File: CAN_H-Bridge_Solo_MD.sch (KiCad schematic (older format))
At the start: 45 parts, among them IC1 SI8650AB-B-IS1, IC2 A3921KLPTR-T, J2 Conn_01x03, J3 Conn_01x05, J4 Bus_mechaken_PCIexpress_x16_1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, M1 Motor_DC, Q1 IRLB3813PBF, Q2 IRLB3813PBF, Q3 IRLB3813PBF, Q4 IRLB3813PBF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

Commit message: change
FETのドレイン端子を移動
パッドを手はんだ用に変更
PCIeコネクタを変更
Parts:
- C1, C10, C11, C12, C13, C2, C3, C4, C5, C6, C7, C8, C9: footprint Capacitor_SMD:C_0805_2012Metric -> Capacitor_SMD:C_0805_2012Metric_Pad1.15x1.40mm_HandSolder
- D1, D2, D3, D4: footprint LED_SMD:LED_0603_1608Metric -> LED_SMD:LED_0603_1608Metric_Castellated
- D5: footprint Diode_SMD:D_0603_1608Metric -> LED_SMD:LED_0603_1608Metric_Castellated
- J4: footprint PCIe:BUS_mechaken_PCIexpress_x16_164_Position -> PCIe:BUS_mechaken_PCIexpress_x16
- R1, R10, R11, R12, R2, R3, R4, R5, R6, R7, R8, R9: footprint Resistor_SMD:R_0603_1608Metric -> Resistor_SMD:R_0603_1608Metric_Pad1.05x0.95mm_HandSolder
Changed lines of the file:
@@
 F 0 "R10" H 10470 4946 50  0000 L CNN
 F 1 "3K" H 10470 4855 50  0000 L CNN
-F 2 "Resistor_SMD:R_0603_1608Metric" V 10330 4900 50  0001 C CNN
+F 2 "Resistor_SMD:R_0603_1608Metric_Pad1.05x0.95mm_HandSolder" V 10330 4900 50  0001 C CNN
 F 3 "~" H 10400 4900 50  0001 C CNN
 	1    10400 4900
@@
 F 0 "R12" H 10930 4854 50  0000 R CNN
 F 1 "2.2k" H 10930 4945 50  0000 R CNN
-F 2 "Resistor_SMD:R_0603_1608Metric" V 10930 4900 50  0001 C CNN
+F 2 "Resistor_SMD:R_0603_1608Metric_Pad1.05x0.95mm_HandSolder" V 10930 4900 50  0001 C CNN
 F 3 "~" H 11000 4900 50  0001 C CNN
 	1    11000 4900
@@
 F 0 "R11" H 10770 4946 50  0000 L CNN
 F 1 "10k" H 10770 4855 50  0000 L CNN
-F 2 "Resistor_SMD:R_0603_1608Metric" V 10630 4900 50  0001 C CNN
+F 2 "Resistor_SMD:R_0603_1608Metric_Pad1.05x0.95mm_HandSolder" V 10630 4900 50  0001 C CNN
 F 3 "~" H 10700 4900 50  0001 C CNN
 	1    10700 4900
@@
 F 0 "C12" H 10015 5446 50  0000 L CNN
 F 1 "0.1uF" H 10015 5355 50  0000 L CNN
-F 2 "Capacitor_SMD:C_0805_2012Metric" H 9938 5250 50  0001 C CNN
+F 2 "Capacitor_SMD:C_0805_2012Metric_Pad1.15x1.40mm_HandSolder" H 9938 5250 50  0001 C CNN
 F 3 "~" H 9900 5400 50  0001 C CNN
 	1    9900 5400
@@
 F 0 "C9" H 7565 5846 50  0000 L CNN
 F 1 "0.1uF" H 7565 5755 50  0000 L CNN
-F 2 "Capacitor_SMD:C_0805_2012Metric" H 7488 5650 50  0001 C CNN
+F 2 "Capacitor_SMD:C_0805_2012Metric_Pad1.15x1.40mm_HandSolder" H 7488 5650 50  0001 C CNN
 F 3 "~" H 7450 5800 50  0001 C CNN
 	1    7450 5800
@@
 F 0 "D5" H 7300 5866 50  0000 C CNN
 F 1 "D" H 7300 5775 50  0000 C CNN
-F 2 "Diode_SMD:D_0603_1608Metric" H 7300 5650 50  0001 C CNN
+F 2 "LED_SMD:LED_0603_1608Metric_Castellated" H 7300 5650 50  0001 C CNN
 F 3 "~" H 7300 5650 50  0001 C CNN
 	1    7300 5650
@@
 F 0 "C5" V 5648 3950 50  0000 C CNN
 F 1 "0.1uF" V 5739 3950 50  0000 C CNN
-F 2 "Capacitor_SMD:C_0805_2012Metric" H 5938 3800 50  0001 C CNN
+F 2 "Capacitor_SMD:C_0805_2012Metric_Pad1.15x1.40mm_HandSolder" H 5938 3800 50  0001 C CNN
 F 3 "~" H 5900 3950 50  0001 C CNN
 	1    5900 3950
@@
 F 0 "C4" V 4248 4600 50  0000 C CNN
 F 1 "0.1uF" V 4339 4600 50  0000 C CNN
-F 2 "Capacitor_SMD:C_0805_2012Metric" H 4538 4450 50  0001 C CNN
+F 2 "Capacitor_SMD:C_0805_2012Metric_Pad1.15x1.40mm_HandSolder" H 4538 4450 50  0001 C CNN
 F 3 "~" H 4500 4600 50  0001 C CNN
 	1    4500 4600
@@
 F 0 "C1" V 748 1800 50  0000 C CNN
 F 1 "1uF" V 839 1800 50  0000 C CNN
-F 2 "Capacitor_SMD:C_0805_2012Metric" H 1038 1650 50  0001 C CNN
+F 2 "Capacitor_SMD:C_0805_2012Metric_Pad1.15x1.40mm_HandSolder" H 1038 1650 50  0001 C CNN
 F 3 "~" H 1000 1800 50  0001 C CNN
 	1    1000 1800
@@
 F 0 "C2" V 1448 1800 50  0000 C CNN
 F 1 "4.7uF" V 1539 1800 50  0000 C CNN
-F 2 "Capacitor_SMD:C_0805_2012Metric" H 1738 1650 50  0001 C CNN
+F 2 "Capacitor_SMD:C_0805_2012Metric_Pad1.15x1.40mm_HandSolder" H 1738 1650 50  0001 C CNN
 F 3 "~" H 1700 1800 50  0001 C CNN
 	1    1700 1800
@@
 F 0 "D1" V 1039 3450 50  0000 C CNN
 F 1 "LED" V 948 3450 50  0000 C CNN
-F 2 "LED_SMD:LED_0603_1608Metric" H 1000 3300 50  0001 C CNN
+F 2 "LED_SMD:LED_0603_1608Metric_Castellated" H 1000 3300 50  0001 C CNN
 F 3 "~" H 1000 3300 50  0001 C CNN
 	1    1000 3300
@@
 F 0 "C3" V 3848 1150 50  0000 C CNN
 F 1 "0.1uF" V 3939 1150 50  0000 C CNN
-F 2 "Capacitor_SMD:C_0805_2012Metric" H 4138 1000 50  0001 C CNN
+F 2 "Capacitor_SMD:C_0805_2012Metric_Pad1.15x1.40mm_HandSolder" H 4138 1000 50  0001 C CNN
 F 3 "~" H 4100 1150 50  0001 C CNN
 	1    4100 1150
@@
 F 0 "R5" V 2443 3100 50  0000 C CNN
 F 1 "10K" V 2534 3100 50  0000 C CNN
-F 2 "Resistor_SMD:R_0603_1608Metric" V 2580 3100 50  0001 C CNN
+F 2 "Resistor_SMD:R_0603_1608Metric_Pad1.05x0.95mm_HandSolder" V 2580 3100 50  0001 C CNN
 F 3 "~" H 2650 3100 50  0001 C CNN
 	1    2650 3100
@@
 F 0 "C7" H 7264 4854 50  0000 L CNN
 F 1 "4.7uF" H 7264 4945 50  0000 L CNN
-F 2 "Capacitor_SMD:C_0805_2012Metric" H 7188 4750 50  0001 C CNN
+F 2 "Capacitor_SMD:C_0805_2012Metric_Pad1.15x1.40mm_HandSolder" H 7188 4750 50  0001 C CNN
 F 3 "~" H 7150 4900 50  0001 C CNN
 	1    7150 4900
@@
 F 0 "C8" H 6823 5446 50  0000 L CNN
 F 1 "4.7uF" H 6823 5355 50  0000 L CNN
-F 2 "Capacitor_SMD:C_0805_2012Metric" H 7188 5250 50  0001 C CNN
+F 2 "Capacitor_SMD:C_0805_2012Metric_Pad1.15x1.40mm_HandSolder" H 7188 5250 50  0001 C CNN
 F 3 "~" H 7150 5400 50  0001 C CNN
 	1    7150 5400
@@
 F 0 "C10" H 9074 5754 50  0000 L CNN
 F 1 "0.47uF" H 9074 5845 50  0000 L CNN
-F 2 "Capacitor_SMD:C_0805_2012Metric" H 9488 5650 50  0001 C CNN
+F 2 "Capacitor_SMD:C_0805_2012Metric_Pad1.15x1.40mm_HandSolder" H 9488 5650 50  0001 C CNN
 F 3 "~" H 9450 5800 50  0001 C CNN
 	1    9450 5800
@@
 F 0 "R4" V 2550 6974 50  0000 L CNN
 F 1 "21" V 2450 6974 50  0000 L CNN
-F 2 "Resistor_SMD:R_0603_1608Metric" V 2280 7050 50  0001 C CNN
+F 2 "Resistor_SMD:R_0603_1608Metric_Pad1.05x0.95mm_HandSolder" V 2280 7050 50  0001 C CNN
 F 3 "~" H 2350 7050 50  0001 C CNN
 	1    2350 7050
@@
 F 0 "C6" H 6415 5046 50  0000 L CNN
 F 1 "4.7uF" H 6415 4955 50  0000 L CNN
-F 2 "Capacitor_SMD:C_0805_2012Metric" H 6338 4850 50  0001 C CNN
+F 2 "Capacitor_SMD:C_0805_2012Metric_Pad1.15x1.40mm_HandSolder" H 6338 4850 50  0001 C CNN
 F 3 "~" H 6300 5000 50  0001 C CNN
 	1    6300 5000
@@
 F 0 "D4" V 3939 5133 50  0000 R CNN
 F 1 "LED" V 3848 5133 50  0000 R CNN
-F 2 "LED_SMD:LED_0603_1608Metric" H 3900 5250 50  0001 C CNN
+F 2 "LED_SMD:LED_0603_1608Metric_Castellated" H 3900 5250 50  0001 C CNN
 F 3 "~" H 3900 5250 50  0001 C CNN
 	1    3900 5250
@@
 F 0 "D3" V 3589 5133 50  0000 R CNN
 F 1 "LED" V 3498 5133 50  0000 R CNN
-F 2 "LED_SMD:LED_0603_1608Metric" H 3550 5250 50  0001 C CNN
+F 2 "LED_SMD:LED_0603_1608Metric_Castellated" H 3550 5250 50  0001 C CNN
 F 3 "~" H 3550 5250 50  0001 C CNN
 	1    3550 5250
@@
 F 0 "J4" H 7600 6800 50  0000 C CNN
 F 1 "Bus_mechaken_PCIexpress_x16_164_Position" H 7550 5400 50  0000 C CNN
-F 2 "PCIe:BUS_mechaken_PCIexpress_x16_164_Position" H 7250 3600 50  0001 C CNN
+F 2 "PCIe:BUS_mechaken_PCIexpress_x16" H 7250 3600 50  0001 C CNN
 F 3 "http://pinouts.ru/Slots/PCI_pinout.shtml" H 7250 3600 50  0001 C CNN
 	1    7600 3700
@@
 F 0 "C11" V 9648 3150 50  0000 C CNN
 F 1 "1uF" V 9739 3150 50  0000 C CNN
-F 2 "Capacitor_SMD:C_0805_2012Metric" H 9938 3000 50  0001 C CNN
+F 2 "Capacitor_SMD:C_0805_2012Metric_Pad1.15x1.40mm_HandSolder" H 9938 3000 50  0001 C CNN
 F 3 "~" H 9900 3150 50  0001 C CNN
 	1    9900 3150
@@
 F 0 "C13" V 10348 3150 50  0000 C CNN
 F 1 "4.7uF" V 10439 3150 50  0000 C CNN
-F 2 "Capacitor_SMD:C_0805_2012Metric" H 10638 3000 50  0001 C CNN
+F 2 "Capacitor_SMD:C_0805_2012Metric_Pad1.15x1.40mm_HandSolder" H 10638 3000 50  0001 C CNN
 F 3 "~" H 10600 3150 50  0001 C CNN
 	1    10600 3150
@@
 F 0 "R2" H 1370 2896 50  0000 L CNN
 F 1 "2.2K" H 1370 2805 50  0000 L CNN
-F 2 "Resistor_SMD:R_0603_1608Metric" V 1230 2850 50  0001 C CNN
+F 2 "Resistor_SMD:R_0603_1608Metric_Pad1.05x0.95mm_HandSolder" V 1230 2850 50  0001 C CNN
 F 3 "~" H 1300 2850 50  0001 C CNN
 	1    1300 2850
@@
 F 0 "R1" H 1070 2896 50  0000 L CNN
 F 1 "2.2K" H 1070 2805 50  0000 L CNN
-F 2 "Resistor_SMD:R_0603_1608Metric" V 930 2850 50  0001 C CNN
+F 2 "Resistor_SMD:R_0603_1608Metric_Pad1.05x0.95mm_HandSolder" V 930 2850 50  0001 C CNN
 F 3 "~" H 1000 2850 50  0001 C CNN
 	1    1000 2850
@@
 F 0 "D2" V 1339 3112 50  0000 C CNN
 F 1 "LED" V 1248 3112 50  0000 C CNN
-F 2 "LED_SMD:LED_0603_1608Metric" H 1300 3300 50  0001 C CNN
+F 2 "LED_SMD:LED_0603_1608Metric_Castellated" H 1300 3300 50  0001 C CNN
 F 3 "~" H 1300 3300 50  0001 C CNN
 	1    1300 3300
@@
 F 0 "R9" V 4815 6975 50  0000 L CNN
 F 1 "21" V 4906 6975 50  0000 L CNN
-F 2 "Resistor_SMD:R_0603_1608Metric" V 4630 7050 50  0001 C CNN
+F 2 "Resistor_SMD:R_0603_1608Metric_Pad1.05x0.95mm_HandSolder" V 4630 7050 50  0001 C CNN
 F 3 "~" H 4700 7050 50  0001 C CNN
 	1    4700 7050
@@
 F 0 "R3" V 2550 6275 50  0000 L CNN
 F 1 "21" V 2450 6275 50  0000 L CNN
-F 2 "Resistor_SMD:R_0603_1608Metric" V 2280 6350 50  0001 C CNN
+F 2 "Resistor_SMD:R_0603_1608Metric_Pad1.05x0.95mm_HandSolder" V 2280 6350 50  0001 C CNN
 F 3 "~" H 2350 6350 50  0001 C CNN
 	1    2350 6350
@@
 F 0 "R8" V 4815 6276 50  0000 L CNN
 F 1 "21" V 4906 6276 50  0000 L CNN
-F 2 "Resistor_SMD:R_0603_1608Metric" V 4630 6350 50  0001 C CNN
+F 2 "Resistor_SMD:R_0603_1608Metric_Pad1.05x0.95mm_HandSolder" V 4630 6350 50  0001 C CNN
 F 3 "~" H 4700 6350 50  0001 C CNN
 	1    4700 6350
@@
 F 0 "R6" H 3620 4996 50  0000 L CNN
 F 1 "2.2K" H 3620 4905 50  0000 L CNN
-F 2 "Resistor_SMD:R_0603_1608Metric" V 3480 4950 50  0001 C CNN
+F 2 "Resistor_SMD:R_0603_1608Metric_Pad1.05x0.95mm_HandSolder" V 3480 4950 50  0001 C CNN
 F 3 "~" H 3550 4950 50  0001 C CNN
 	1    3550 4950
@@
 F 0 "R7" H 3970 4996 50  0000 L CNN
 F 1 "2.2K" H 3970 4905 50  0000 L CNN
-F 2 "Resistor_SMD:R_0603_1608Metric" V 3830 4950 50  0001 C CNN
+F 2 "Resistor_SMD:R_0603_1608Metric_Pad1.05x0.95mm_HandSolder" V 3830 4950 50  0001 C CNN
 F 3 "~" H 3900 4950 50  0001 C CNN
 	1    3900 4950

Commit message: change
レギュレータを新規に追加
その他細かな修正
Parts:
- added C14: 2.2u, Capacitor_SMD:C_0805_2012Metric_Pad1.15x1.40mm_HandSolder, symbol Device:C
- added C15: 1u, Capacitor_SMD:C_0805_2012Metric_Pad1.15x1.40mm_HandSolder, symbol Device:C
- added IC3: AP7381-50SA-7, SOT96P240X105-3N, symbol SamacSys_Parts:AP7381-50SA-7
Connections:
- wire segments 101 -> 107
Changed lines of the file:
@@
 	1    0    0    -1
 $EndComp
+$Comp
+L SamacSys_Parts:AP7381-50SA-7 IC3
+U 1 1 5E2DF031
+P 9650 2200
+F 0 "IC3" H 10200 2465 50  0000 C CNN
+F 1 "AP7381-50SA-7" H 10200 2374 50  0000 C CNN
+F 2 "SOT96P240X105-3N" H 10600 2300 50  0001 L CNN
+F 3 "https://componentsearchengine.com/Datasheets/1/AP7381-50SA-7.pdf" H 10600 2200 50  0001 L CNN
+F 4 "LDO Voltage Regulators LDO CMOS LowCurr SOT23 T&R 3K" H 10600 2100 50  0001 L CNN "Description"
+F 5 "1.05" H 10600 2000 50  0001 L CNN "Height"
+F 6 "621-AP7381-50SA-7" H 10600 1900 50  0001 L CNN "Mouser Part Number"
+F 7 "https://www.mouser.com/Search/Refine.aspx?Keyword=621-AP7381-50SA-7" H 10600 1800 50  0001 L CNN "Mouser Price/Stock"
+F 8 "Diodes Inc." H 10600 1700 50  0001 L CNN "Manufacturer_Name"
+F 9 "AP7381-50SA-7" H 10600 1600 50  0001 L CNN "Manufacturer_Part_Number"
+	1    9650 2200
+	1    0    0    -1
+$EndComp
+$Comp
+L power:GNDPWR #PWR0101
+U 1 1 5E2DFCDA
+P 10750 2600
+F 0 "#PWR0101" H 10750 2400 50  0001 C CNN
+F 1 "GNDPWR" H 10754 2446 50  0000 C CNN
+F 2 "" H 10750 2550 50  0001 C CNN
+F 3 "" H 10750 2550 50  0001 C CNN
+	1    10750 2600
+	1    0    0    -1
+$EndComp
+$Comp
+L Device:C C15
+U 1 1 5E2E38F9
+P 9400 2350
+F 0 "C15" H 9285 2304 50  0000 R CNN
+F 1 "1u" H 9285 2395 50  0000 R CNN
+F 2 "Capacitor_SMD:C_0805_2012Metric_Pad1.15x1.40mm_HandSolder" H 9438 2200 50  0001 C CNN
+F 3 "~" H 9400 2350 50  0001 C CNN
+	1    9400 2350
+	-1   0    0    1
+$EndComp
+$Comp
+L Device:C C14
+U 1 1 5E2E6C2C
+P 9200 2450
+F 0 "C14" H 9315 2404 50  0000 L CNN
+F 1 "2.2u" H 9315 2495 50  0000 L CNN
+F 2 "Capacitor_SMD:C_0805_2012Metric_Pad1.15x1.40mm_HandSolder" H 9238 2300 50  0001 C CNN
+F 3 "~" H 9200 2450 50  0001 C CNN
+	1    9200 2450
+	-1   0    0    1
+$EndComp
+Wire Wire Line
+	9650 2200 9400 2200
+Wire Wire Line
+	9200 2600 9400 2600
+Wire Wire Line
+	10750 2600 10750 2200
+Connection ~ 10750 2600
+Wire Wire Line
+	9200 2300 9650 2300
+Wire Wire Line
+	9400 2500 9400 2600
+Connection ~ 9400 2600
+Wire Wire Line
+	9400 2600 10750 2600
+$Comp
+L power:VCC #PWR011
+U 1 1 5E308F85
+P 9400 2200
+F 0 "#PWR011" H 9400 2050 50  0001 C CNN
+F 1 "VCC" H 9417 2373 50  0000 C CNN
+F 2 "" H 9400 2200 50  0001 C CNN
+F 3 "" H 9400 2200 50  0001 C CNN
+	1    9400 2200
+	0    -1   -1   0
+$EndComp
+Text GLabel 9200 2300 0    50   Output ~ 0
+MD_3V3
 $EndSCHEMATC

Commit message: clean
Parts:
- IC3: symbol SamacSys_Parts:AP7381-50SA-7 -> CAN_H-Bridge_Solo_MD-rescue:AP7381-50SA-7-SamacSys_Parts
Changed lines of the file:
@@
 $EndComp
 $Comp
-L SamacSys_Parts:AP7381-50SA-7 IC3
+L CAN_H-Bridge_Solo_MD-rescue:AP7381-50SA-7-SamacSys_Parts IC3
 U 1 1 5E2DF031
 P 9650 2200

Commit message: release
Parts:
- Q1, Q2, Q3, Q4: value IRLB3813PBF -> IRFB3806PBF
- R1, R2, R6, R7: value 2.2K -> 2.2k
- R10: value 3K -> 3k
- R5: value 10K -> 10k
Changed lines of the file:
@@
 P 10400 4900
 F 0 "R10" H 10470 4946 50  0000 L CNN
-F 1 "3K" H 10470 4855 50  0000 L CNN
+F 1 "3k" H 10470 4855 50  0000 L CNN
 F 2 "Resistor_SMD:R_0603_1608Metric_Pad1.05x0.95mm_HandSolder" V 10330 4900 50  0001 C CNN
 F 3 "~" H 10400 4900 50  0001 C CNN
@@
 P 2650 3100
 F 0 "R5" V 2443 3100 50  0000 C CNN
-F 1 "10K" V 2534 3100 50  0000 C CNN
+F 1 "10k" V 2534 3100 50  0000 C CNN
 F 2 "Resistor_SMD:R_0603_1608Metric_Pad1.05x0.95mm_HandSolder" V 2580 3100 50  0001 C CNN
 F 3 "~" H 2650 3100 50  0001 C CNN
@@
 P 1300 2850
 F 0 "R2" H 1370 2896 50  0000 L CNN
-F 1 "2.2K" H 1370 2805 50  0000 L CNN
+F 1 "2.2k" H 1370 2805 50  0000 L CNN
 F 2 "Resistor_SMD:R_0603_1608Metric_Pad1.05x0.95mm_HandSolder" V 1230 2850 50  0001 C CNN
 F 3 "~" H 1300 2850 50  0001 C CNN
@@
 P 1000 2850
 F 0 "R1" H 1070 2896 50  0000 L CNN
-F 1 "2.2K" H 1070 2805 50  0000 L CNN
+F 1 "2.2k" H 1070 2805 50  0000 L CNN
 F 2 "Resistor_SMD:R_0603_1608Metric_Pad1.05x0.95mm_HandSolder" V 930 2850 50  0001 C CNN
 F 3 "~" H 1000 2850 50  0001 C CNN
@@
 P 2700 7050
 F 0 "Q2" H 2904 7096 50  0000 L CNN
-F 1 "IRLB3813PBF" H 2904 7005 50  0000 L CNN
+F 1 "IRFB3806PBF" H 2904 7005 50  0000 L CNN
 F 2 "Package_TO_SOT_THT:TO-220-3_Vertical" H 2950 6975 50  0001 L CIN
 F 3 "http://www.infineon.com/dgdl/irlb8721pbf.pdf?fileId=5546d462533600a40153566056732591" H 2700 7050 50  0001 L CNN
@@
 P 4350 7050
 F 0 "Q4" H 4554 7096 50  0000 L CNN
-F 1 "IRLB3813PBF" H 4554 7005 50  0000 L CNN
+F 1 "IRFB3806PBF" H 4554 7005 50  0000 L CNN
 F 2 "Package_TO_SOT_THT:TO-220-3_Vertical" H 4600 6975 50  0001 L CIN
 F 3 "http://www.infineon.com/dgdl/irlb8721pbf.pdf?fileId=5546d462533600a40153566056732591" H 4350 7050 50  0001 L CNN
@@
 P 2700 6350
 F 0 "Q1" H 2904 6396 50  0000 L CNN
-F 1 "IRLB3813PBF" H 2904 6305 50  0000 L CNN
+F 1 "IRFB3806PBF" H 2904 6305 50  0000 L CNN
 F 2 "Package_TO_SOT_THT:TO-220-3_Vertical" H 2950 6275 50  0001 L CIN
 F 3 "http://www.infineon.com/dgdl/irlb8721pbf.pdf?fileId=5546d462533600a40153566056732591" H 2700 6350 50  0001 L CNN
@@
 P 4350 6350
 F 0 "Q3" H 4554 6396 50  0000 L CNN
-F 1 "IRLB3813PBF" H 4554 6305 50  0000 L CNN
+F 1 "IRFB3806PBF" H 4554 6305 50  0000 L CNN
 F 2 "Package_TO_SOT_THT:TO-220-3_Vertical" H 4600 6275 50  0001 L CIN
 F 3 "http://www.infineon.com/dgdl/irlb8721pbf.pdf?fileId=5546d462533600a40153566056732591" H 4350 6350 50  0001 L CNN
@@
 P 3550 4950
 F 0 "R6" H 3620 4996 50  0000 L CNN
-F 1 "2.2K" H 3620 4905 50  0000 L CNN
+F 1 "2.2k" H 3620 4905 50  0000 L CNN
 F 2 "Resistor_SMD:R_0603_1608Metric_Pad1.05x0.95mm_HandSolder" V 3480 4950 50  0001 C CNN
 F 3 "~" H 3550 4950 50  0001 C CNN
@@
 P 3900 4950
 F 0 "R7" H 3970 4996 50  0000 L CNN
-F 1 "2.2K" H 3970 4905 50  0000 L CNN
+F 1 "2.2k" H 3970 4905 50  0000 L CNN
 F 2 "Resistor_SMD:R_0603_1608Metric_Pad1.05x0.95mm_HandSolder" V 3830 4950 50  0001 C CNN
 F 3 "~" H 3900 4950 50  0001 C CNN

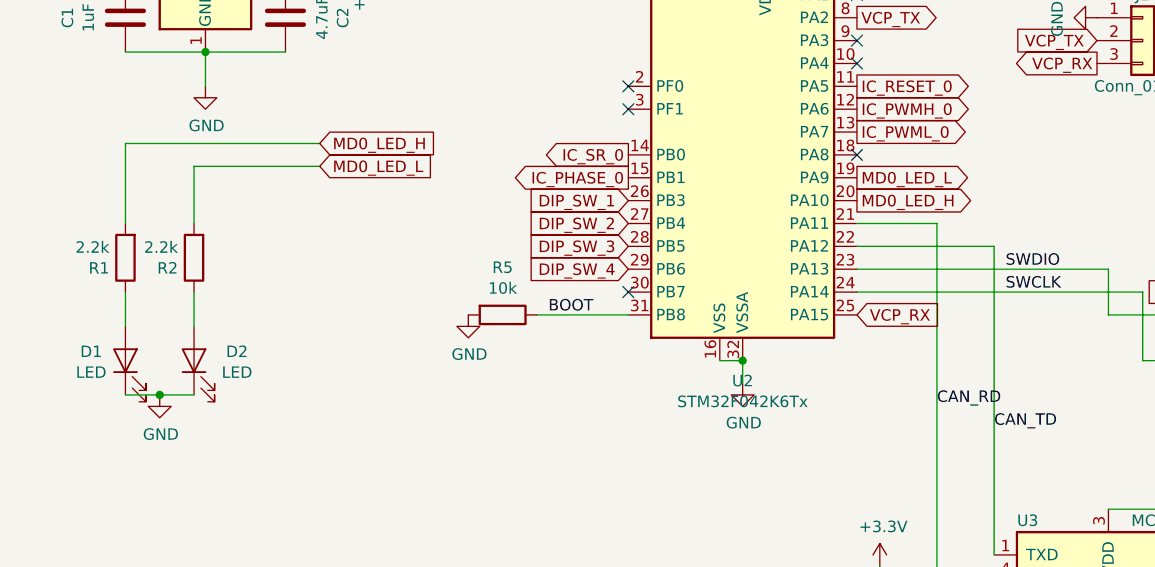
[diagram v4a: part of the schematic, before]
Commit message: clean
LEDの配線を変更
PA9 <-> PA10
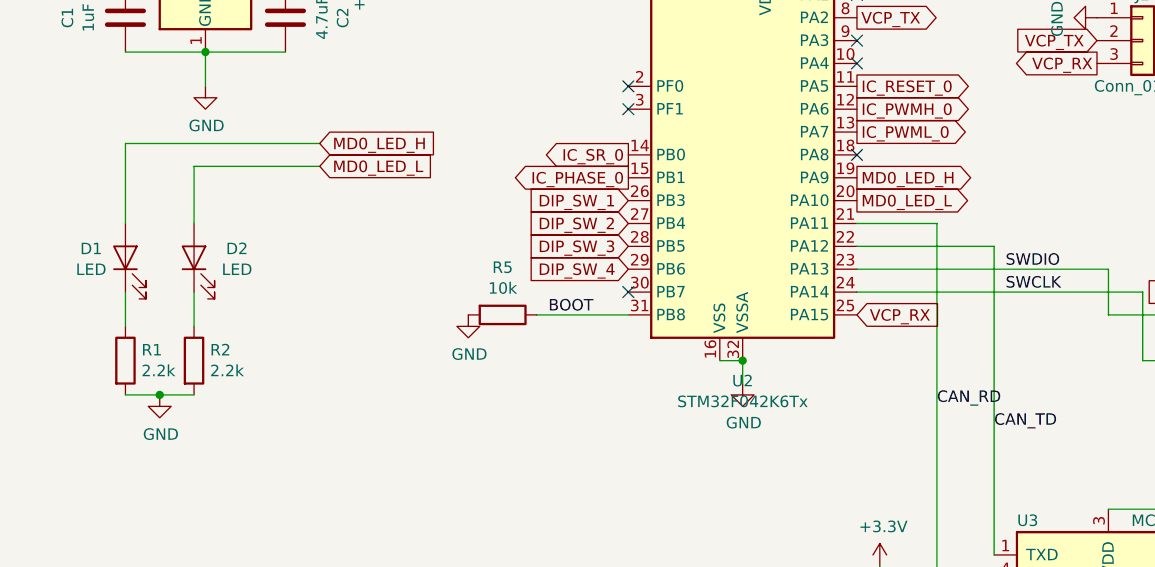
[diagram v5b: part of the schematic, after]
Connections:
- net GND: now also R1.2, R2.2; no longer D1.1 (K), D2.1 (K)
- net MD0_LED_H: now also D1.2 (A), U2.19 (PA9); no longer R1.2, U2.20 (PA10)
- net MD0_LED_L: now also D2.2 (A), U2.20 (PA10); no longer R2.2, U2.19 (PA9)
- net at R2.1: now also D2.1 (K); no longer D2.2 (A)
- net at R1.1: now also D1.1 (K); no longer D1.2 (A)
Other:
- moved on the sheet: D1, D2, R1, R2
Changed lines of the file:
@@
 L Device:LED D1
 U 1 1 5D5ECBC3
-P 1000 3300
-F 0 "D1" V 1039 3450 50  0000 C CNN
-F 1 "LED" V 948 3450 50  0000 C CNN
-F 2 "LED_SMD:LED_0603_1608Metric_Castellated" H 1000 3300 50  0001 C CNN
-F 3 "~" H 1000 3300 50  0001 C CNN
-	1    1000 3300
+P 1000 2850
+F 0 "D1" V 1039 3000 50  0000 C CNN
+F 1 "LED" V 948 3000 50  0000 C CNN
+F 2 "LED_SMD:LED_0603_1608Metric_Castellated" H 1000 2850 50  0001 C CNN
+F 3 "~" H 1000 2850 50  0001 C CNN
+	1    1000 2850
 	0    -1   -1   0
 $EndComp
@@
 Text GLabel 5300 1150 0    50   Output ~ 0
 DIP_SW_4
-Text GLabel 1850 2350 2    50   Input ~ 0
-MD0_LED_H
-Text GLabel 1850 2450 2    50   Input ~ 0
-MD0_LED_L
 Text GLabel 3200 2900 0    50   Input ~ 0
 DIP_SW_4
@@
 Text GLabel 4200 2200 2    50   Output ~ 0
 IC_PWMH_0
+Text GLabel 4200 2500 2    50   Output ~ 0
+MD0_LED_H
 Text GLabel 4200 2600 2    50   Output ~ 0
-MD0_LED_H
-Text GLabel 4200 2500 2    50   Output ~ 0
 MD0_LED_L
 $Comp
@@
 L Device:R R2
 U 1 1 5E0C5428
+P 1300 3300
+F 0 "R2" H 1370 3346 50  0000 L CNN
+F 1 "2.2k" H 1370 3255 50  0000 L CNN
+F 2 "Resistor_SMD:R_0603_1608Metric_Pad1.05x0.95mm_HandSolder" V 1230 3300 50  0001 C CNN
+F 3 "~" H 1300 3300 50  0001 C CNN
+	1    1300 3300
+	1    0    0    -1
+$EndComp
+$Comp
+L Device:R R1
+U 1 1 5E0C542E
+P 1000 3300
+F 0 "R1" H 1070 3346 50  0000 L CNN
+F 1 "2.2k" H 1070 3255 50  0000 L CNN
+F 2 "Resistor_SMD:R_0603_1608Metric_Pad1.05x0.95mm_HandSolder" V 930 3300 50  0001 C CNN
+F 3 "~" H 1000 3300 50  0001 C CNN
+	1    1000 3300
+	1    0    0    -1
+$EndComp
+Wire Wire Line
+	1300 3450 1150 3450
+$Comp
+L Device:LED D2
+U 1 1 5D5EBAF7
 P 1300 2850
-F 0 "R2" H 1370 2896 50  0000 L CNN
-F 1 "2.2k" H 1370 2805 50  0000 L CNN
-F 2 "Resistor_SMD:R_0603_1608Metric_Pad1.05x0.95mm_HandSolder" V 1230 2850 50  0001 C CNN
+F 0 "D2" V 1339 2662 50  0000 C CNN
+F 1 "LED" V 1248 2662 50  0000 C CNN
+F 2 "LED_SMD:LED_0603_1608Metric_Castellated" H 1300 2850 50  0001 C CNN
 F 3 "~" H 1300 2850 50  0001 C CNN
 	1    1300 2850
-	-1   0    0    1
-$EndComp
-$Comp
-L Device:R R1
-U 1 1 5E0C542E
-P 1000 2850
-F 0 "R1" H 1070 2896 50  0000 L CNN
-F 1 "2.2k" H 1070 2805 50  0000 L CNN
-F 2 "Resistor_SMD:R_0603_1608Metric_Pad1.05x0.95mm_HandSolder" V 930 2850 50  0001 C CNN
-F 3 "~" H 1000 2850 50  0001 C CNN
-	1    1000 2850
-	-1   0    0    1
-$EndComp
-Wire Wire Line
-	1300 3450 1150 3450
-$Comp
-L Device:LED D2
-U 1 1 5D5EBAF7
-P 1300 3300
-F 0 "D2" V 1339 3112 50  0000 C CNN
-F 1 "LED" V 1248 3112 50  0000 C CNN
-F 2 "LED_SMD:LED_0603_1608Metric_Castellated" H 1300 3300 50  0001 C CNN
-F 3 "~" H 1300 3300 50  0001 C CNN
-	1    1300 3300
 	0    -1   -1   0
 $EndComp
@@
 Text GLabel 9200 2300 0    50   Output ~ 0
 MD_3V3
+Text GLabel 1850 2350 2    50   Input ~ 0
+MD0_LED_H
+Text GLabel 1850 2450 2    50   Input ~ 0
+MD0_LED_L
 $EndSCHEMATC
